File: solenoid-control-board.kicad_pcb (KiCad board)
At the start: 2 copper layers, 72 x 48 mm, 39 parts, among them J1 505578-0671, J2 505578-0671, J3 SM04B-GHS-TB, J4 XT30PW-M30.G.Y1, J5 XT30PW-M30.G.Y1, M1 CSD16323Q3, M2 CSD16323Q3, M3 CSD16323Q3, M4 CSD16323Q3, M5 CSD16323Q3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

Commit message: Working on layout
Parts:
- moved R7 16.0 mm to (136.0, 65.1), turned to -90 degrees
- moved D1 11.4 mm to (160.0, 77.0)
- moved D2 11.4 mm to (158.0, 77.1)
- moved D3 11.4 mm to (156.0, 77.1)
- moved D4 11.4 mm to (143.2, 82.5)
- moved D5 11.4 mm to (151.9, 76.7)
- moved D6 11.4 mm to (149.9, 76.7)
- moved D8 11.4 mm to (145.5, 77.1), turned to 90 degrees
- moved R1 11.4 mm to (160.0, 80.4)
- moved R2 11.4 mm to (158.0, 80.4)
- moved R3 11.4 mm to (156.0, 80.4)
- moved R4 11.4 mm to (154.0, 80.6)
- moved R5 11.4 mm to (151.9, 79.9)
- moved R6 11.4 mm to (149.9, 79.9)
- moved R8 11.4 mm to (145.5, 80.4)
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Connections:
- J4 pad 3: unconnected-(J4-Pad3) -> GND
- J4 pad 4: unconnected-(J4-Pad4) -> GND
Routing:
- net GATE_5: track 0.00 -> 27.6 mm, vias 0 -> 2
- net GATE_4: track 0.00 -> 26.7 mm, vias 0 -> 1
- net GATE_6: track 0.00 -> 21.5 mm, vias 0 -> 2
- net SDA: track 0.00 -> 18.4 mm
- net SRC_4: track 0.00 -> 14.4 mm
- net I2C_PWR: track 0.00 -> 12.9 mm
- net GND: track 0.12 -> 11.4 mm, vias 8 -> 9
- net SCK: track 0.00 -> 11.1 mm
- net SRC_5: track 7.28 -> 15.0 mm
- net I2C_GND: track 0.00 -> 7.64 mm
- net SRC_6: track 7.30 -> 14.2 mm
- net Net-(D10-Pad1): track 0.00 -> 4.52 mm
- net Net-(D11-Pad1): track 0.00 -> 2.30 mm
- net Net-(D9-Pad1): track 0.00 -> 2.30 mm
- net Net-(D7-Pad1): track 0.00 -> 2.29 mm
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- added copper zone on F.Cu, net SOL_6_PWR
- added copper zone on F.Cu, net SRC_5
- added copper zone on F.Cu, net SRC_6
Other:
- outline, holes or cut-outs redrawn

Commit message: Finished almost everything
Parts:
- moved R5 16.3 mm to (146.6, 64.5), turned to -90 degrees
- moved R1 16.1 mm to (162.6, 64.5), turned to -90 degrees
- moved R3 15.9 mm to (154.6, 64.5), turned to -90 degrees
- moved D4 14.5 mm to (154.6, 73.5), turned to -90 degrees
- moved D5 9.76 mm to (146.6, 68.5), turned to 90 degrees
- moved D1 8.86 mm to (162.6, 68.5), turned to 90 degrees
- moved D3 8.73 mm to (154.6, 68.5), turned to 90 degrees
- moved D8 7.79 mm to (138.6, 73.5), turned to -90 degrees
- moved R8 7.46 mm to (138.6, 77.5)
- moved D2 5.86 mm to (162.6, 73.5)
- moved R2 5.42 mm to (162.6, 77.5)
- moved D6 4.60 mm to (146.6, 73.5)
- moved J1 4.49 mm to (150.0, 90.0)
- moved R6 4.12 mm to (146.6, 77.5)
- moved H1 3.99 mm to (155.3, 58.0), turned to -90 degrees
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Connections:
- H1 pad 1: +6V -> +12V
- H1 pad 2: +6V -> +12V
- H1 pad 3: SRC_1 -> SRC_2
- H1 pad 4: SRC_2 -> SRC_1
- H1 pad 5: +12V -> +6V
- H1 pad 6: +12V -> +6V
- H2 pad 1: +6V -> +12V
- H2 pad 2: +6V -> +12V
- H2 pad 3: SRC_3 -> SRC_4
- H2 pad 4: SRC_4 -> SRC_3
- H2 pad 5: +12V -> +6V
- H2 pad 6: +12V -> +6V
- H3 pad 1: +6V -> +12V
- H3 pad 2: +6V -> +12V
- H3 pad 3: SRC_5 -> SRC_6
- H3 pad 4: SRC_6 -> SRC_5
- H3 pad 5: +12V -> +6V
- H3 pad 6: +12V -> +6V
- J1 pad 1: SOL_3_PWR -> GND
- J1 pad 2: GND -> SOL_3_PWR
- J1 pad 3: SOL_2_PWR -> GND
- J1 pad 4: GND -> SOL_2_PWR
- J1 pad 5: SOL_1_PWR -> GND
- J1 pad 6: GND -> SOL_1_PWR
- J2 pad 1: SOL_6_PWR -> GND
- J2 pad 2: GND -> SOL_6_PWR
- J2 pad 3: SOL_5_PWR -> GND
- J2 pad 4: GND -> SOL_5_PWR
- J2 pad 5: SOL_4_PWR -> GND
- J2 pad 6: GND -> SOL_4_PWR
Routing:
- net GATE_1: track 0.00 -> 59.0 mm, vias 0 -> 2
- net GATE_2: track 0.00 -> 51.8 mm, vias 0 -> 2
- net GATE_3: track 0.00 -> 44.7 mm, vias 0 -> 2
- net SRC_3: track 0.00 -> 14.1 mm
- net SRC_2: track 0.00 -> 14.1 mm
- net SRC_1: track 0.00 -> 14.0 mm
- net GATE_4: track 26.7 -> 37.5 mm, vias 1 -> 2
- net GND: track 11.4 -> 20.3 mm, vias 9 -> 6
- net SOL_5_PWR: track 0.00 -> 7.00 mm
- net SOL_4_PWR: track 0.00 -> 7.00 mm
- net SOL_3_PWR: track 0.00 -> 7.00 mm
- net SOL_2_PWR: track 0.00 -> 7.00 mm
- net SOL_1_PWR: track 0.00 -> 7.00 mm
- net SOL_6_PWR: track 1.50 -> 7.00 mm
- net Net-(D6-Pad1): track 0.00 -> 2.91 mm
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- added copper zone on F.Cu, net SOL_1_PWR
- added copper zone on F.Cu, net SOL_2_PWR
- added copper zone on F.Cu, net SOL_3_PWR
- added copper zone on F.Cu, net SOL_4_PWR
- added copper zone on F.Cu, net SOL_5_PWR
- added copper zone on F.Cu, net SRC_1
- added copper zone on F.Cu, net SRC_2
- added copper zone on F.Cu, net SRC_3
- added copper zone on F.Cu, net SRC_4
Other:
- board size 72 x 48 mm -> 75 x 45 mm

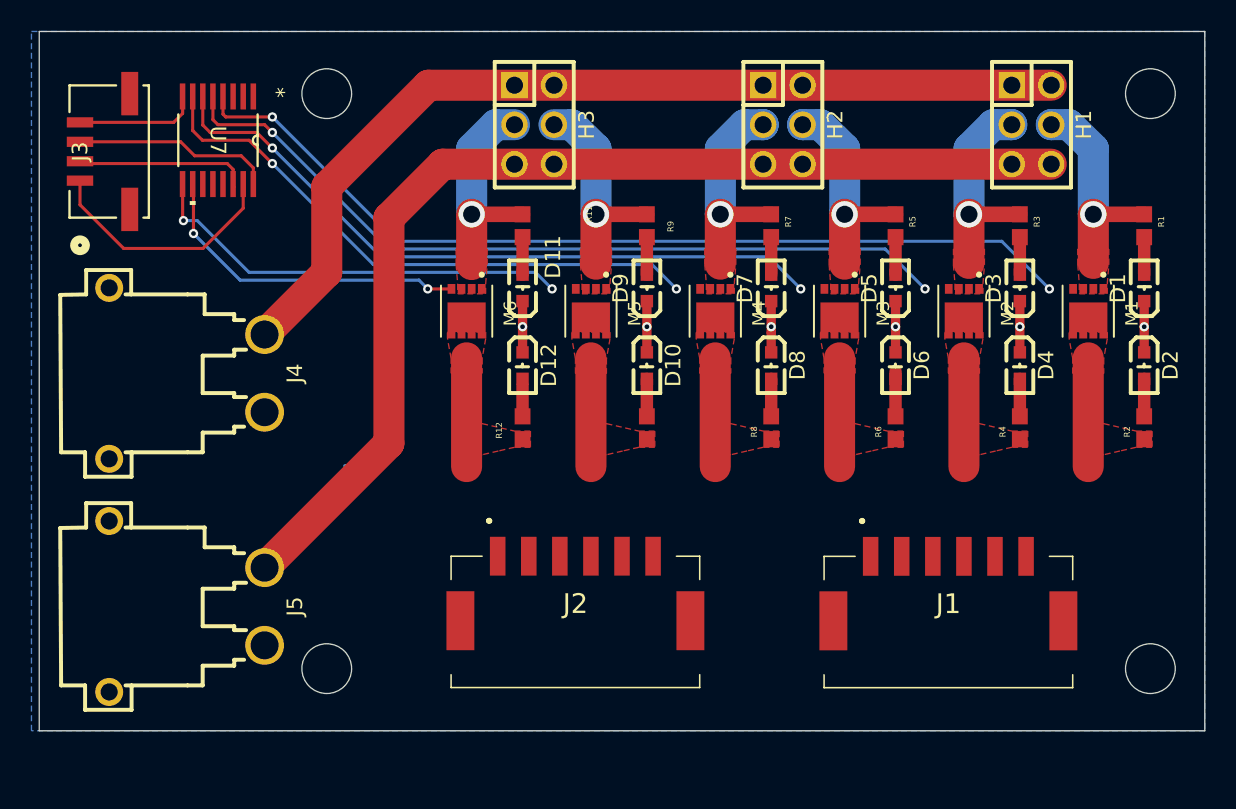
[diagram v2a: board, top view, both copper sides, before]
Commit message: Finished layout, need to simulate
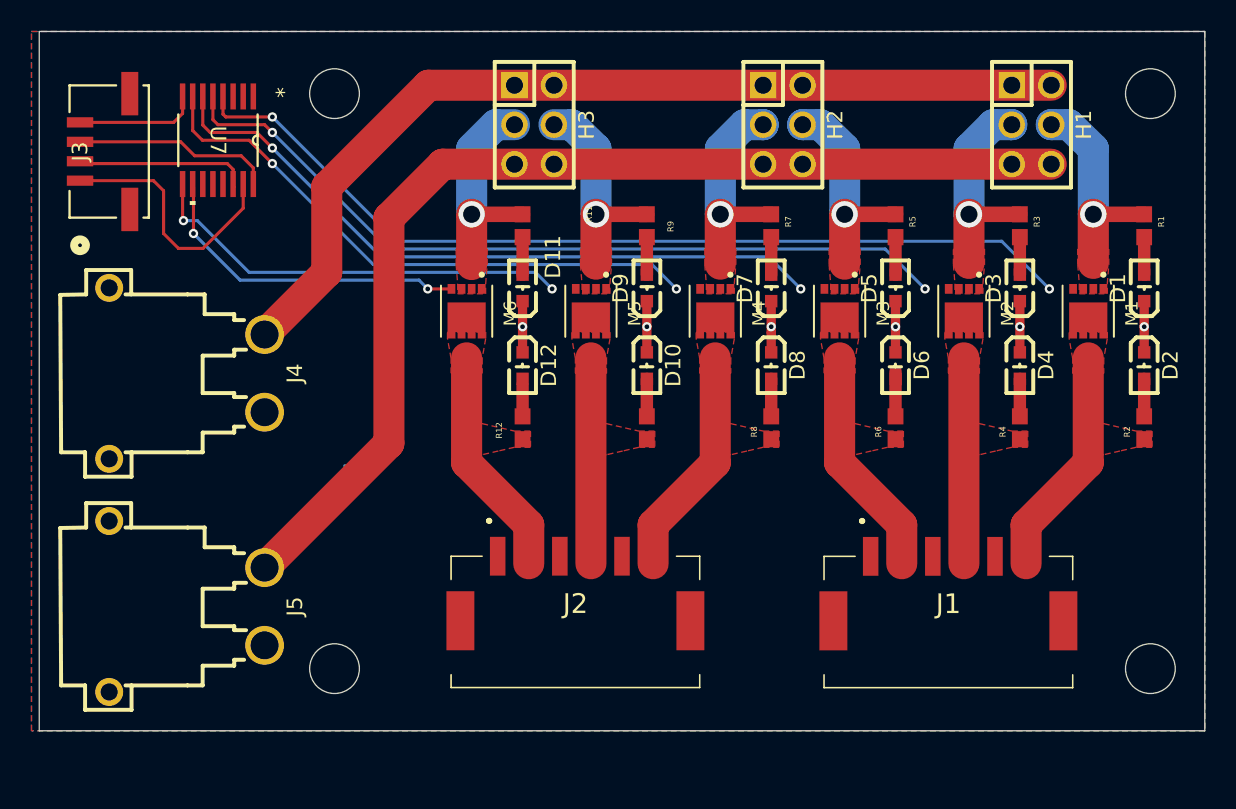
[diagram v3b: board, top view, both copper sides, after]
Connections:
- J1 pad MP1: unconnected-(J1-PadMP1) -> GND
- J1 pad MP2: unconnected-(J1-PadMP2) -> GND
- J2 pad MP1: unconnected-(J2-PadMP1) -> GND
- J2 pad MP2: unconnected-(J2-PadMP2) -> GND
- J3 pad 5: (no net) -> GND
- J3 pad 6: (no net) -> GND
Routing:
- net SOL_6_PWR: track 7.00 -> 14.9 mm
- net SOL_4_PWR: track 7.00 -> 14.9 mm
- net SOL_3_PWR: track 7.00 -> 14.9 mm
- net SOL_1_PWR: track 7.00 -> 14.9 mm
- net SOL_5_PWR: track 7.00 -> 13.2 mm
- net SOL_2_PWR: track 7.00 -> 13.2 mm
- net SDA: track 15.7 -> 16.4 mm
- added copper zone on F.Cu, net GND
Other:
- outline, holes or cut-outs redrawn

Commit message: Fixed DRCs
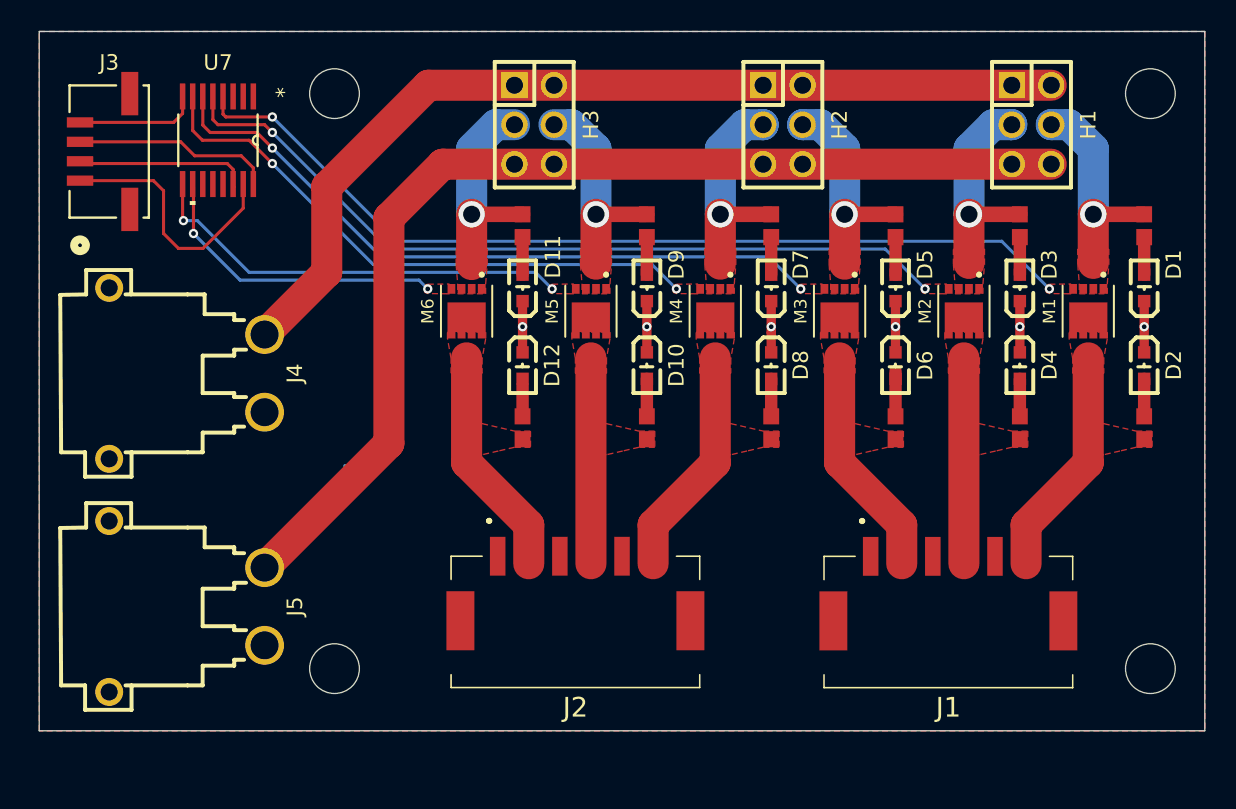
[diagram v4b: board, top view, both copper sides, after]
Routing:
- net GATE_6: track 21.0 -> 19.6 mm
- added copper zone on F.Cu, net GATE_1
- added copper zone on F.Cu, net GATE_2
- added copper zone on F.Cu, net GATE_3
- added copper zone on F.Cu, net GATE_4
- added copper zone on F.Cu, net GATE_5
- added copper zone on F.Cu, net GATE_6

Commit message: Generated BOM
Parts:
- D1, D11, D3, D5, D7, D9: footprint Downloaded:LED0603-R-RD_ORANGE -> solenoid-control-board:LED0603-R-RD_ORANGE
- D10, D12, D2, D4, D6, D8: footprint Downloaded:LED0603-R-RD_GREEN -> solenoid-control-board:LED0603-R-RD_GREEN
- H1, H2, H3: value ~ -> HX PZ2.54-2x3P ZZ; footprint Downloaded:HDR-TH_6P-P2.54-V-M-R2-C3-S2.54-2 -> solenoid-control-board:HDR-TH_6P-P2.54-V-M-R2-C3-S2.54-2
- J1, J2: footprint Downloaded:5055780671 -> solenoid-control-board:5055780671
- J3: footprint Downloaded:CONN_SM04B-GHS-TB_JST -> solenoid-control-board:CONN_SM04B-GHS-TB_JST
- J4, J5: value XT30PW-M30.G.Y1 -> XT30PW-M30.G.Y; footprint Downloaded:CONN-TH_XT30PW-M -> solenoid-control-board:CONN-TH_XT30PW-M
- M1, M2, M3, M4, M5, M6: footprint Downloaded:TRANS_CSD17308Q3 -> solenoid-control-board:TRANS_CSD17308Q3
- R1, R10, R11, R12, R2, R3, R4, R5, R6, R7, R8, R9: value 4.7kΩ -> R; footprint Downloaded:RESC1607X60N -> solenoid-control-board:RESC1607X60N
- U7: footprint Downloaded:PW16 -> solenoid-control-board:PW16
